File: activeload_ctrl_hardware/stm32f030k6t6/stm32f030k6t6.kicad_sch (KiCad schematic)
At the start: 43 parts

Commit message: stm32f0k6t6 scheme
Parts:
- removed C? (x2): 100u, Capacitor_THT:CP_Radial_D4.0mm_P2.00mm, symbol Device:CP
- removed C?: 470u 25v, Capacitor_THT:C_Radial_D8.0mm_H7.0mm_P3.50mm, symbol Device:CP
- removed R?: 10k, Resistor_SMD:R_1206_3216Metric_Pad1.30x1.75mm_HandSolder, symbol Device:R
- removed RN? (x4): 10k, Resistor_SMD:R_Array_Convex_4x1206, symbol Device:R_Pack04_Split
- removed SW?: (no value), Rotary_Encoder:RotaryEncoder_Alps_EC12E-Switch_Vertical_H20mm, symbol Device:Rotary_Encoder_Switch
- removed U?: AMS1117-5.0, Package_TO_SOT_SMD:SOT-223-3_TabPin2, symbol Regulator_Linear:AMS1117-5.0
- removed U?: STM32F030F4Px, Package_SO:TSSOP-20_4.4x6.5mm_P0.65mm, symbol MCU_ST_STM32F0:STM32F030F4Px
- removed U?: AMS1117-3.3, Package_TO_SOT_SMD:SOT-223-3_TabPin2, symbol Regulator_Linear:AMS1117-3.3
- added C5: 470u, Capacitor_THT:C_Radial_D8.0mm_H7.0mm_P3.50mm, symbol Device:C_Polarized
- added C7, C9: 100u, Capacitor_THT:CP_Radial_D4.0mm_P2.00mm, symbol Device:C_Polarized
- added C?: 0.1u, Capacitor_SMD:C_0805_2012Metric_Pad1.18x1.45mm_HandSolder, symbol Device:C
- added J4: USART, Connector_PinHeader_2.54mm:PinHeader_1x03_P2.54mm_Vertical, symbol Connector_Generic:Conn_01x03
- added R1, R2, R3, R4, R5: 10k, Resistor_SMD:R_1206_3216Metric_Pad1.30x1.75mm_HandSolder, symbol Device:R
- added SW1: ~, Rotary_Encoder:RotaryEncoder_Alps_EC12E-Switch_Vertical_H20mm, symbol Device:RotaryEncoder_Switch
- added U3: AMS1117-5.0, Package_TO_SOT_SMD:SOT-223-3_TabPin2, symbol Regulator_Linear:AMS1117-5.0
- added U4: AMS1117-3.3, Package_TO_SOT_SMD:SOT-223-3_TabPin2, symbol Regulator_Linear:AMS1117-3.3
- added U?: STM32F030K6Tx, Package_QFP:LQFP-32_7x7mm_P0.8mm, symbol MCU_ST_STM32F0:STM32F030K6Tx
- gave numbers to parts that had none: 31
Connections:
- net +3.3VADC: now also U?.5 (VDDA)
- net +5V: now also C7.1, U3.2 (VO)
- net BTN1: now also R4.2, U?.15 (PB1)
- net BTN2: now also R5.2, U?.26 (PB3)
- net BTN3: now also U?.27 (PB4)
- net ENC_A: now also U?.12 (PA6)
- net ENC_B: now also U?.13 (PA7)
- net ENC_BTN: now also R3.2, SW1.S1, U?.14 (PB0)
- net GND: now also C5.2, C7.2, C9.2, C?.2, J4.3 (Pin_3), SW1.C, SW1.S2, U3.1 (GND), U4.1 (GND), U?.16 (VSS), U?.32 (VSS)
- net I2C_SCL: now also U?.19 (PA9)
- net I2C_SDA: now also U?.20 (PA10)
- net LED_G: now also U?.29 (PB6)
- net LED_R: now also U?.30 (PB7)
- net LED_Y: now also U?.28 (PB5)
- net RESET: now also U?.4 (NRST)
- net SWCLK: now also U?.25 (PA15)
- net SWDIO: now also U?.24 (PA14)
- net USART_RX: now also J4.2 (Pin_2), U?.9 (PA3)
- net USART_TX: now also J4.1 (Pin_1), U?.8 (PA2)
- net WOE: now also U?.3 (PF1)
- net ~{WOE}: now also U?.2 (PF0)
- net at R8.1: now also R1.2, SW1.A
- net at R10.1: now also U?.31 (BOOT0)
- net at R9.1: now also R2.2, SW1.B
- net +3V3 renamed +3.3V
- net +3.3V: now also C9.1, C?.1, R1.1, R2.1, R3.1, R4.1, R5.1, U4.2 (VO), U?.1 (VDD), U?.17 (VDD)
- net +VPS renamed +12V
- net +12V: now also C5.1, U3.3 (VI), U4.3 (VI)
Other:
- note added: "Control elements"
- note added: "Indication"
- note added: "MCU&EEPROM"
- note added: "Output connection"
- moved on the sheet: C1, C10, C11, C2, C3, C4, C6, C8, D1, D2, D3, J1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

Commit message: stm32f030k6t6 scheme and model cube mx
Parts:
- gave numbers to parts that had none: 2
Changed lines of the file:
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@@
 			(font
 				(size 2.54 2.54)
-				(thickness 0.508)
-				(bold yes)
-				(italic yes)
 			)
 			(justify left bottom)
@@
 			(font
 				(size 2.54 2.54)
-				(thickness 0.508)
-				(bold yes)
-				(italic yes)
 			)
 			(justify left bottom)
@@
 			(font
 				(size 2.54 2.54)
-				(thickness 0.508)
-				(bold yes)
-				(italic yes)
 			)
 			(justify left bottom)
@@
 			(font
 				(size 2.54 2.54)
-				(thickness 0.508)
-				(bold yes)
-				(italic yes)
 			)
 			(justify left bottom)
@@
 			(font
 				(size 2.54 2.54)
-				(thickness 0.508)
-				(bold yes)
-				(italic yes)
 			)
 			(justify left bottom)
@@
 		(on_board yes)
 		(dnp no)
-		(property "Reference" "C?"
+		(property "Reference" "C12"
 			(at 29.591 29.3116 0)
 			(effects
@@
 			(project "stm32f030k6t6"
 				(path "/d7d9441b-f478-4590-87f0-c9f097cf72ee"
-					(reference "C?")
+					(reference "C12")
 					(unit 1)
 				)
@@
 		(on_board yes)
 		(dnp no)
-		(fields_autoplaced yes)
-		(property "Reference" "U?"
-			(at 77.1241 86.8101 0)
+		(property "Reference" "U1"
+			(at 79.248 35.4217 0)
 			(effects
 				(font
@@
 		)
 		(property "Value" "STM32F030K6Tx"
-			(at 77.1241 89.2344 0)
+			(at 79.248 37.846 0)
 			(effects
 				(font
@@
 			(project ""
 				(path "/d7d9441b-f478-4590-87f0-c9f097cf72ee"
-					(reference "U?")
-					(unit 1)
-				)
+					(reference "U1")
+					(unit 1)
+				)

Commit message: stm32f030k6t6 pcb
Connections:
- no-connect marks 0 -> 8
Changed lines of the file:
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@@
 		(color 0 0 0 0)
+	)
+	(no_connect
+		(at 87.63 62.23)
+	)
+	(no_connect
+		(at 87.63 69.85)
+	)
+	(no_connect
+		(at 87.63 54.61)
+	)
+	(no_connect
+		(at 87.63 74.93)
+	)
+	(no_connect
+		(at 87.63 44.45)
+	)
+	(no_connect
+		(at 87.63 52.07)
+	)
+	(no_connect
+		(at 87.63 41.91)
+	)
+	(no_connect
+		(at 87.63 72.39)
 	)
 	(wire

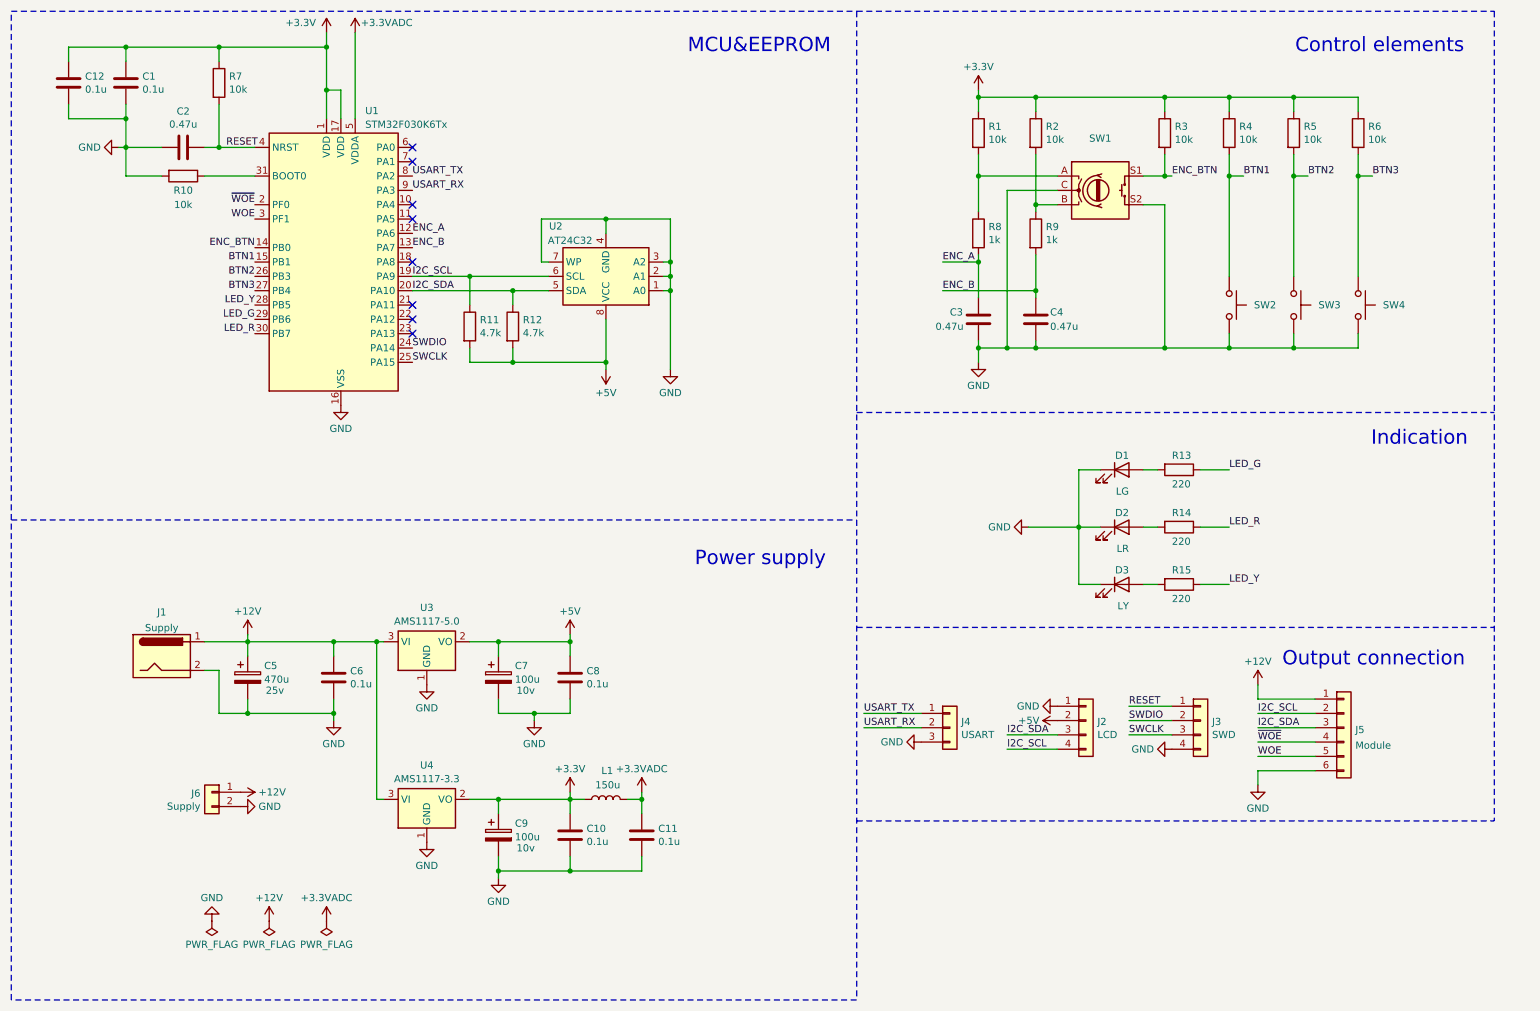
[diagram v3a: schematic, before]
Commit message: stm32f030k6t6 pcb
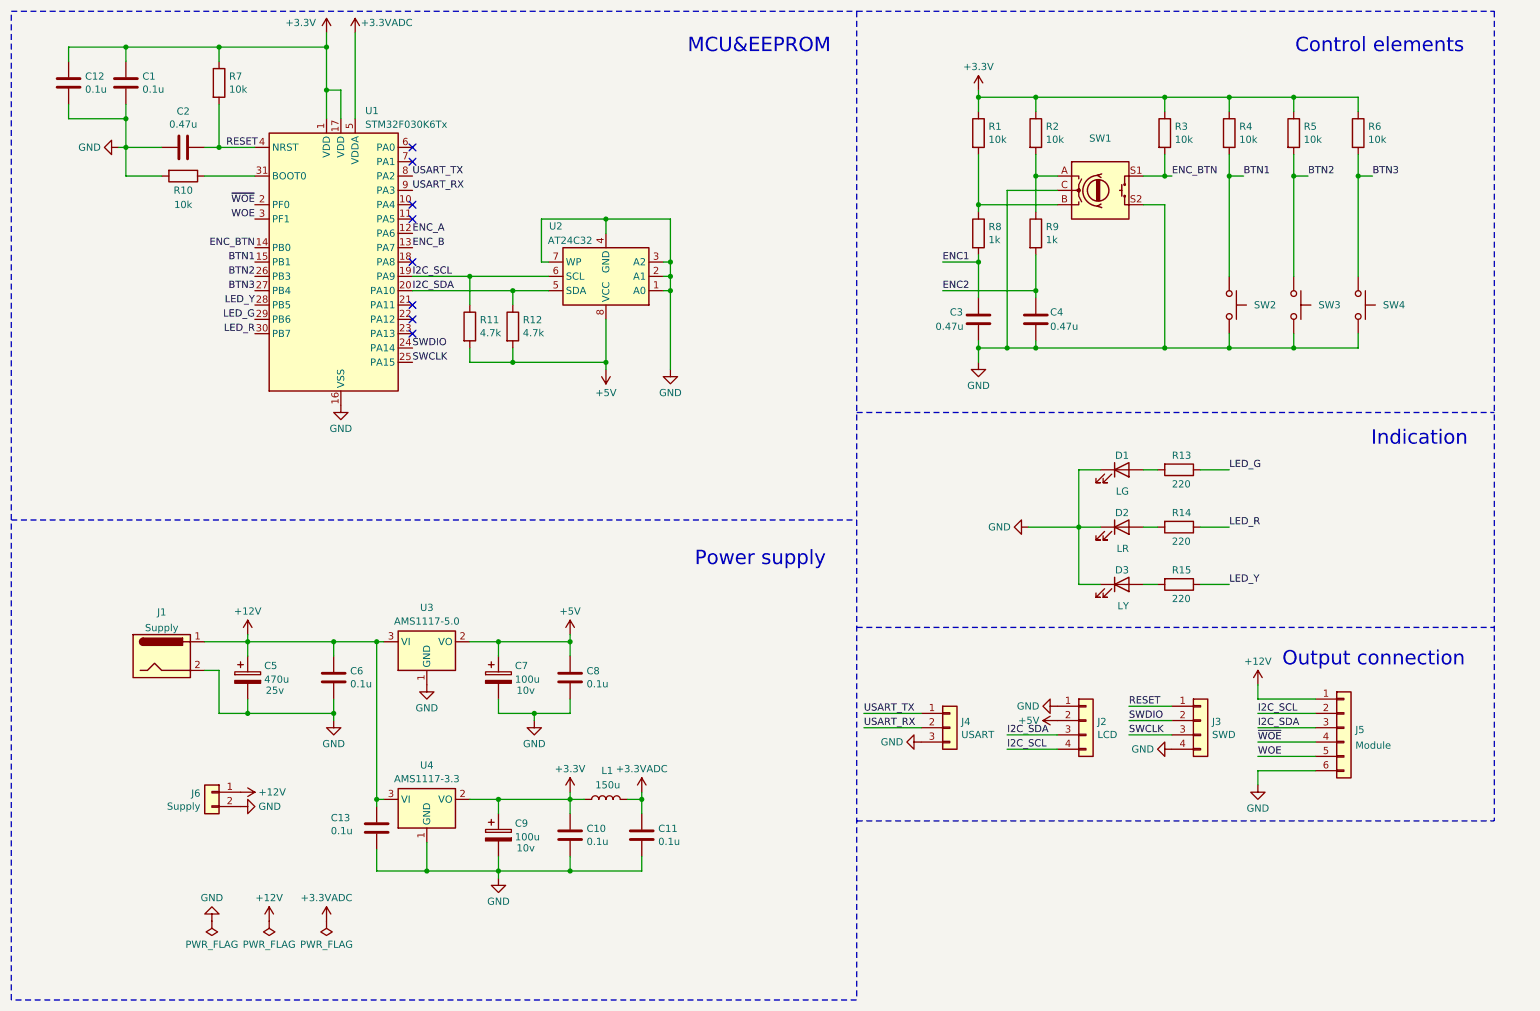
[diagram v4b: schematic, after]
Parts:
- added C13: 0.1u, Capacitor_SMD:C_0805_2012Metric_Pad1.18x1.45mm_HandSolder, symbol Device:C
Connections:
- net +12V: now also C13.1
- net ENC_A: no longer C3.1, R8.2
- net ENC_B: no longer C4.1, R9.2
- net GND: now also C13.2
- net at R1.2, R8.1: now also SW1.B; no longer SW1.A
- net at R2.2, R9.1: now also SW1.A; no longer SW1.B
- new net ENC1: C3.1, R8.2
- new net ENC2: C4.1, R9.2
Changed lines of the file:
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@@
 	)
 	(junction
-		(at 187.96 46.99)
-		(diameter 0)
-		(color 0 0 0 0)
-	)
-	(junction
 		(at 115.57 170.18)
 		(diameter 0)
@@
 	)
 	(junction
+		(at 81.28 157.48)
+		(diameter 0)
+		(color 0 0 0 0)
+	)
+	(junction
 		(at 133.35 67.31)
 		(diameter 0)
@@
 	)
 	(junction
+		(at 187.96 52.07)
+		(diameter 0)
+		(color 0 0 0 0)
+	)
+	(junction
 		(at 36.83 24.13)
 		(diameter 0)
@@
 	)
 	(junction
-		(at 198.12 52.07)
-		(diameter 0)
-		(color 0 0 0 0)
-	)
-	(junction
 		(at 97.79 64.77)
 		(diameter 0)
@@
 	)
 	(junction
+		(at 198.12 46.99)
+		(diameter 0)
+		(color 0 0 0 0)
+	)
+	(junction
 		(at 73.66 142.24)
 		(diameter 0)
@@
 	)
 	(junction
+		(at 90.17 170.18)
+		(diameter 0)
+		(color 0 0 0 0)
+	)
+	(junction
 		(at 102.87 157.48)
 		(diameter 0)
@@
 	(wire
 		(pts
+			(xy 198.12 46.99) (xy 201.93 46.99)
+		)
+		(stroke
+			(width 0)
+			(type default)
+		)
+	)
+	(wire
+		(pts
 			(xy 193.04 77.47) (xy 198.12 77.47)
 		)
@@
 	(wire
 		(pts
+			(xy 187.96 52.07) (xy 187.96 53.34)
+		)
+		(stroke
+			(width 0)
+			(type default)
+		)
+	)
+	(wire
+		(pts
 			(xy 209.55 99.06) (xy 205.74 99.06)
 		)
@@
 		)
 	)
-	(wire
-		(pts
-			(xy 198.12 52.07) (xy 201.93 52.07)
-		)
-		(stroke
-			(width 0)
-			(type default)
-		)
-	)
 	(polyline
 		(pts
@@
 	(wire
 		(pts
+			(xy 81.28 157.48) (xy 81.28 158.75)
+		)
+		(stroke
+			(width 0)
+			(type default)
+		)
+	)
+	(wire
+		(pts
 			(xy 196.85 109.22) (xy 205.74 109.22)
 		)
@@
 	(wire
 		(pts
-			(xy 237.49 152.4) (xy 247.65 152.4)
+			(xy 90.17 165.1) (xy 90.17 170.18)
 		)
 		(stroke
@@
 	(wire
 		(pts
-			(xy 198.12 52.07) (xy 198.12 53.34)
+			(xy 237.49 152.4) (xy 247.65 152.4)
 		)
 		(stroke
@@
 	(wire
 		(pts
-			(xy 187.96 46.99) (xy 187.96 53.34)
-		)
-		(stroke
-			(width 0)
-			(type default)
-		)
-	)
-	(wire
-		(pts
 			(xy 105.41 69.85) (xy 105.41 67.31)
 		)
@@
 	(wire
 		(pts
-			(xy 187.96 46.99) (xy 201.93 46.99)
-		)
-		(stroke
-			(width 0)
-			(type default)
-		)
-	)
-	(wire
-		(pts
 			(xy 50.8 134.62) (xy 53.34 134.62)
 		)
@@
 	(wire
 		(pts
-			(xy 198.12 43.18) (xy 198.12 52.07)
+			(xy 198.12 43.18) (xy 198.12 46.99)
 		)
 		(stroke
@@
 	(wire
 		(pts
+			(xy 198.12 46.99) (xy 198.12 53.34)
+		)
+		(stroke
+			(width 0)
+			(type default)
+		)
+	)
+	(wire
+		(pts
 			(xy 237.49 142.24) (xy 247.65 142.24)
 		)
@@
 	(wire
 		(pts
+			(xy 90.17 170.18) (xy 81.28 170.18)
+		)
+		(stroke
+			(width 0)
+			(type default)
+		)
+	)
+	(wire
+		(pts
 			(xy 255.27 46.99) (xy 255.27 64.77)
 		)
@@
 	(wire
 		(pts
+			(xy 187.96 52.07) (xy 201.93 52.07)
+		)
+		(stroke
+			(width 0)
+			(type default)
+		)
+	)
+	(wire
+		(pts
 			(xy 26.67 24.13) (xy 36.83 24.13)
 		)
@@
 	(wire
 		(pts
+			(xy 81.28 166.37) (xy 81.28 170.18)
+		)
+		(stroke
+			(width 0)
+			(type default)
+		)
+	)
+	(wire
+		(pts
 			(xy 109.22 143.51) (xy 109.22 142.24)
 		)
@@
 	(wire
 		(pts
-			(xy 187.96 43.18) (xy 187.96 46.99)
+			(xy 187.96 43.18) (xy 187.96 52.07)
 		)
 		(stroke
@@
 	(wire
 		(pts
+			(xy 102.87 170.18) (xy 90.17 170.18)
+		)
+		(stroke
+			(width 0)
+			(type default)
+		)
+	)
+	(wire
+		(pts
 			(xy 72.39 21.59) (xy 72.39 24.13)
 		)
@@
 		)
 	)
-	(label "ENC_B"
+	(label "ENC2"
 		(at 181.61 67.31 0)
 		(fields_autoplaced yes)
@@
 		)
 	)
-	(label "ENC_A"
+	(label "ENC1"
 		(at 181.61 62.23 0)
 		(fields_autoplaced yes)
@@
 	)
 	(symbol
-		(lib_name "GND_1")
-		(lib_id "power:GND")
-		(at 90.17 165.1 0)
-		(unit 1)
-		(exclude_from_sim no)
-		(in_bom yes)
-		(on_board yes)
-		(dnp no)
-		(fields_autoplaced yes)
-		(property "Reference" "#PWR025"
-			(at 90.17 171.45 0)
-			(effects
-				(font
-					(size 1.27 1.27)
-				)
-				(hide yes)
-			)
-		)
-		(property "Value" "GND"
-			(at 90.17 169.2331 0)
-			(effects
-				(font
-					(size 1.27 1.27)
-				)
-			)
-		)
-		(property "Footprint" ""
-			(at 90.17 165.1 0)
-			(effects
-				(font
-					(size 1.27 1.27)
-				)
-				(hide yes)
-			)
-		)
-		(property "Datasheet" ""
-			(at 90.17 165.1 0)
-			(effects
-				(font
-					(size 1.27 1.27)
-				)
-				(hide yes)
-			)
-		)
-		(property "Description" "Power symbol creates a global label with name \"GND\" , ground"
-			(at 90.17 165.1 0)
-			(effects
-				(font
-					(size 1.27 1.27)
-				)
-				(hide yes)
-			)
-		)
-		(pin "1"
-		)
-		(instances
-			(project "stm32f030f4p6"
-				(path "/d7d9441b-f478-4590-87f0-c9f097cf72ee"
-					(reference "#PWR025")
-					(unit 1)
-				)
-			)
-		)
-	)
-	(symbol
 		(lib_id "Connector_Generic:Conn_01x02")
 		(at 52.07 156.21 0)
@@
 					(unit 1)
 				)
+			)
+		)
+	)
+	(symbol
+		(lib_id "Device:C")
+		(at 81.28 162.56 0)
+		(unit 1)
+		(exclude_from_sim no)
+		(in_bom yes)
+		(on_board yes)
+		(dnp no)
+		(property "Reference" "C13"
+			(at 73.152 160.7566 0)
+			(effects
+				(font
+					(size 1.27 1.27)
+				)
+				(justify left)
+			)
+		)
+		(property "Value" "0.1u"
+			(at 73.152 163.068 0)
+			(effects
+				(font
+					(size 1.27 1.27)
+				)
+				(justify left)
+			)
+		)
+		(property "Footprint" "Capacitor_SMD:C_0805_2012Metric_Pad1.18x1.45mm_HandSolder"
+			(at 82.2452 166.37 0)
+			(effects
+				(font
+					(size 1.27 1.27)
+				)
+				(hide yes)
+			)
+		)
+		(property "Datasheet" "~"
+			(at 81.28 162.56 0)
+			(effects
+				(font
+					(size 1.27 1.27)
+				)
+				(hide yes)
+			)
+		)
+		(property "Description" ""
+			(at 81.28 162.56 0)
+			(effects
+				(font
+					(size 1.27 1.27)
+				)
+				(hide yes)
+			)
+		)
+		(pin "1"
+		)
+		(pin "2"
+		)
+		(instances
+			(project "stm32f030k6t6"
+				(path "/d7d9441b-f478-4590-87f0-c9f097cf72ee"
+					(reference "C13")
+					(unit 1)
+				)

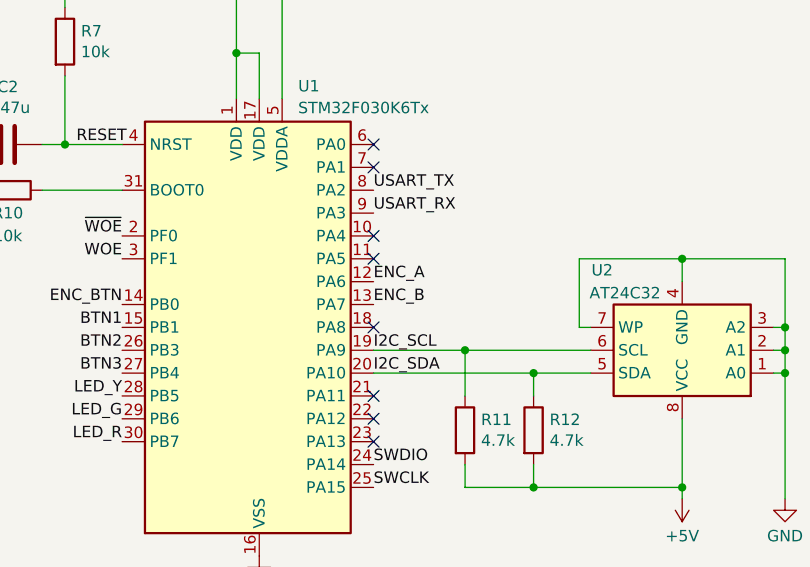
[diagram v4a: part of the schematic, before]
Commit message: stm32f030k6t6 pcb in grogress
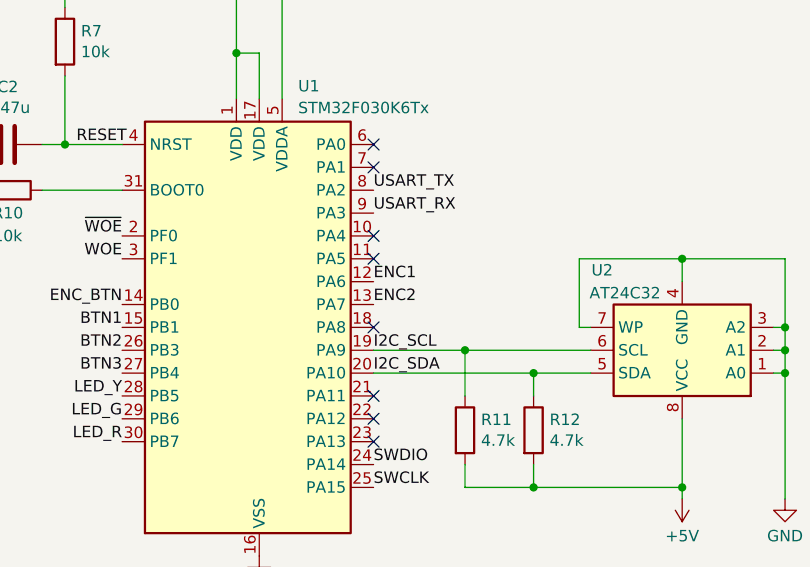
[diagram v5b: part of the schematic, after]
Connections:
- net ENC_A is gone; now on net ENC1: U1.12 (PA6)
- net ENC_B is gone; now on net ENC2: U1.13 (PA7)
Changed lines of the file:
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@@
 		)
 	)
-	(label "ENC_A"
+	(label "ENC1"
 		(at 87.63 57.15 0)
 		(fields_autoplaced yes)
@@
 		)
 	)
-	(label "ENC_B"
+	(label "ENC2"
 		(at 87.63 59.69 0)
 		(fields_autoplaced yes)

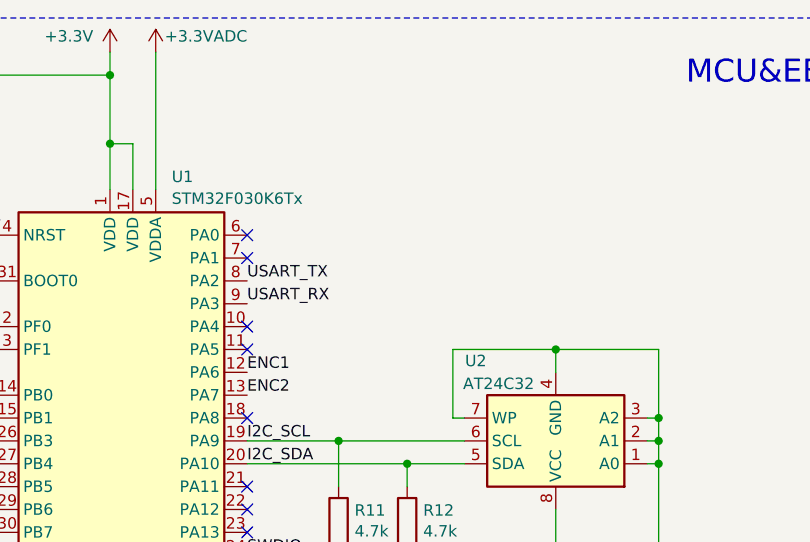
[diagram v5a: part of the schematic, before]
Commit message: stm32f030k6t6  add testpoint to scheme
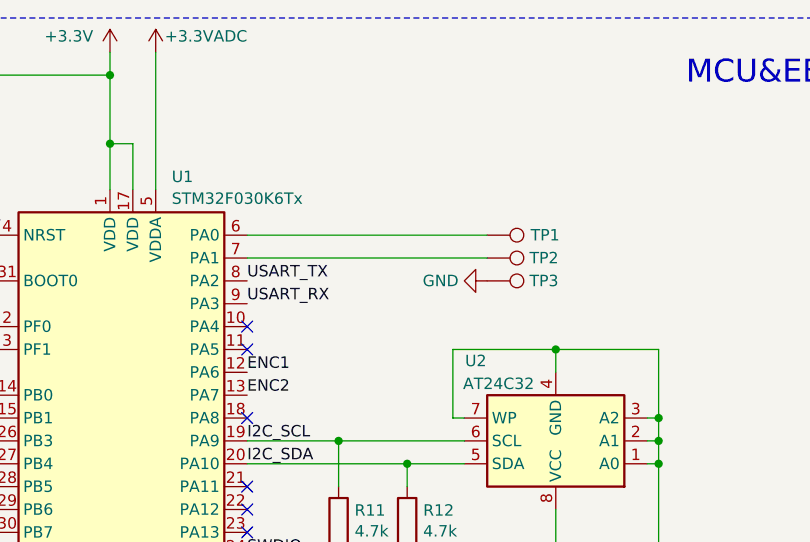
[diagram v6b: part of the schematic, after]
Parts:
- added TP1, TP2, TP3: TestPoint, Connector_PinHeader_2.54mm:PinHeader_1x01_P2.54mm_Vertical, symbol Connector:TestPoint
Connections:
- net GND: now also TP3.1
- net at U1.6 (PA0): now also TP1.1
- net at U1.7 (PA1): now also TP2.1
- no-connect marks 8 -> 6
